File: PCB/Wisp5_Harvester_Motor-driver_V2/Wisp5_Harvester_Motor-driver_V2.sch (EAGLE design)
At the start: 29 parts, among them M1 PINHEAD_PINHD-1X2-1.27MM, M2 PINHEAD_PINHD-1X2-1.27MM, U1 BQ25570

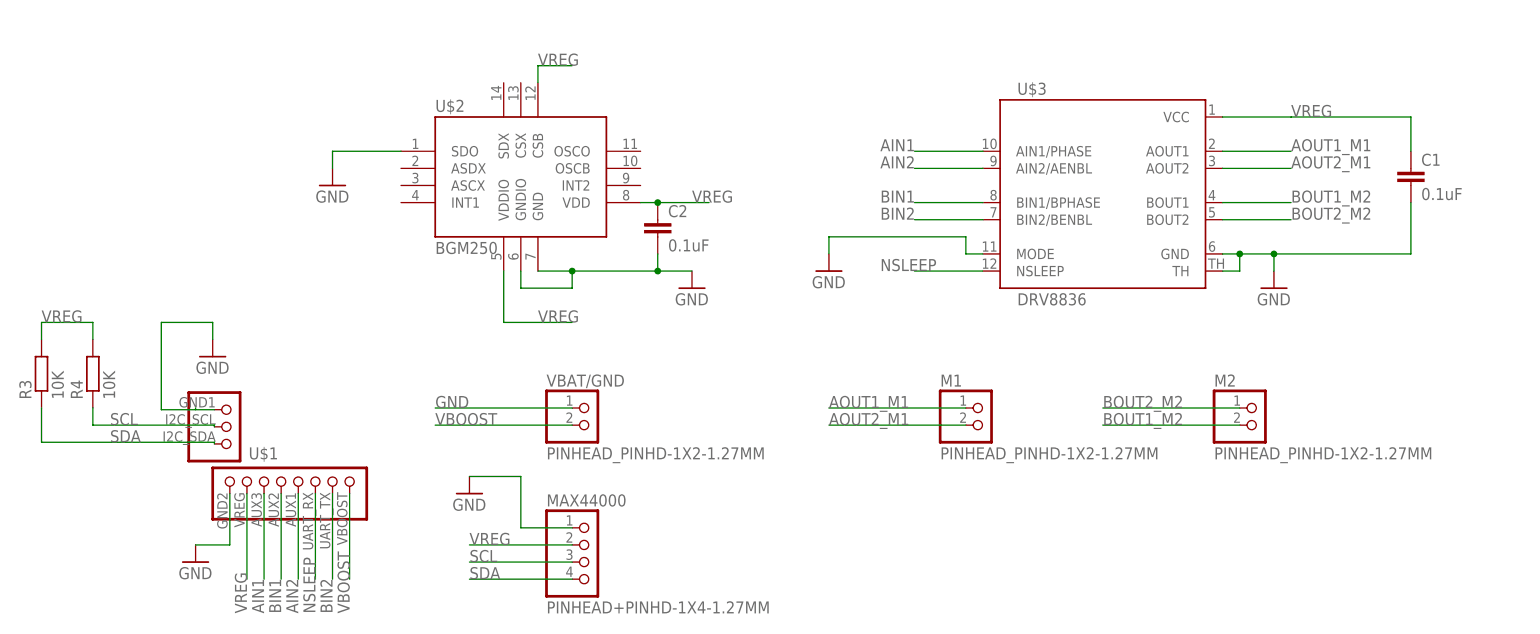
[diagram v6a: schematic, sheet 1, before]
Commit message: Update schematic, added missing scl and sda lines for the gyro
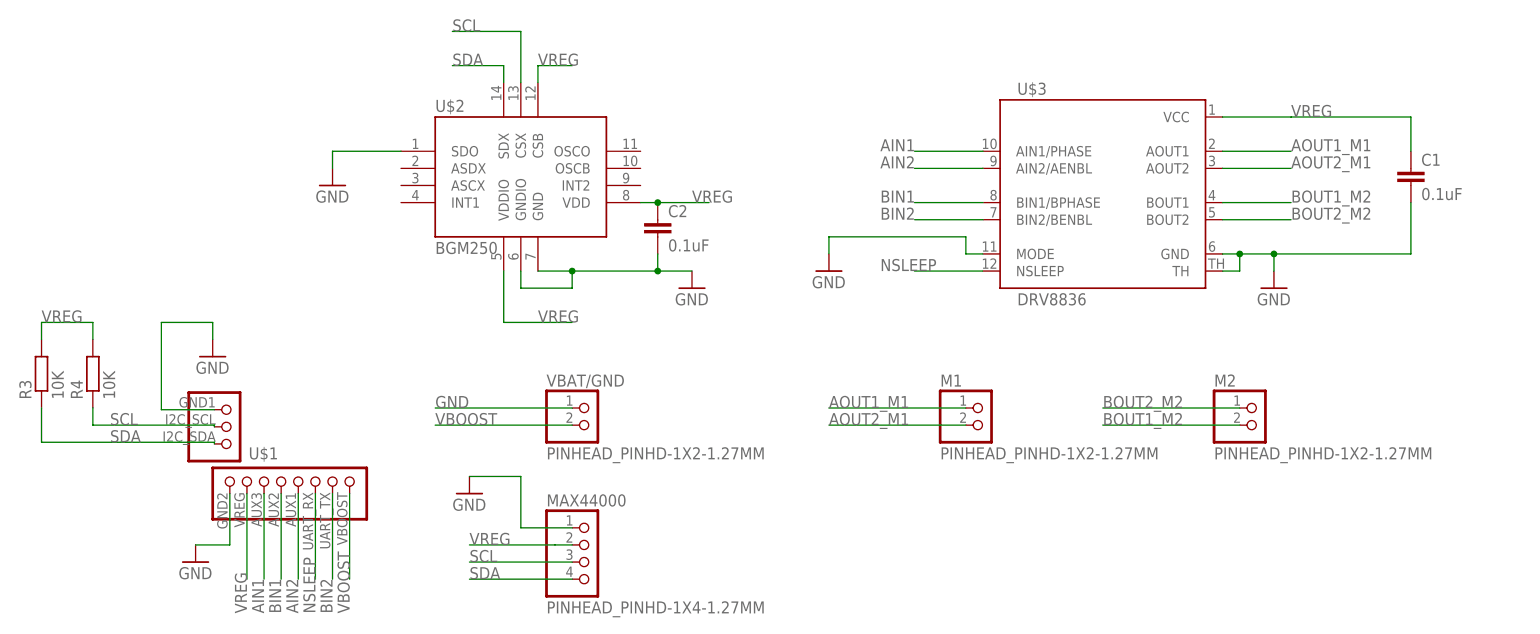
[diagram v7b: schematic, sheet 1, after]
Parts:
- MAX44000: value PINHEAD+PINHD-1X4-1.27MM -> PINHEAD_PINHD-1X4-1.27MM; device Wisp5_Harvester_Motor-driver_V2:PINHEAD+PINHD-1X4-1.27MM -> Wisp5_Harvester_Motor-driver_V2:PINHEAD_PINHD-1X4-1.27MM
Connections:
- net SCL: now also U$2.CSX
- net SDA: now also U$2.SDX
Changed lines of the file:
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@@
 <part name="U$3" library="robot_pcb2" deviceset="DRV8836" device=""/>
 <part name="U1" library="Wisp5_Harvester_Motor-driver_V2" deviceset="BQ25570" device=""/>
-<part name="GND1" library="supply1" deviceset="GND" device=""/>
-<part name="GND5" library="supply1" deviceset="GND" device=""/>
-<part name="C3" library="rcl" deviceset="C-EU" device="C0805" value="4.7uF"/>
-<part name="GND6" library="supply1" deviceset="GND" device=""/>
-<part name="GND7" library="supply1" deviceset="GND" device=""/>
-<part name="C5" library="rcl" deviceset="C-EU" device="C0805" value="10nF"/>
+<part name="GND1" library="supply1" library_urn="urn:adsk.eagle:library:371" deviceset="GND" device=""/>
+<part name="GND5" library="supply1" library_urn="urn:adsk.eagle:library:371" deviceset="GND" device=""/>
+<part name="C3" library="rcl" library_urn="urn:adsk.eagle:library:334" deviceset="C-EU" device="C0805" value="4.7uF"/>
+<part name="GND6" library="supply1" library_urn="urn:adsk.eagle:library:371" deviceset="GND" device=""/>
+<part name="GND7" library="supply1" library_urn="urn:adsk.eagle:library:371" deviceset="GND" device=""/>
+<part name="C5" library="rcl" library_urn="urn:adsk.eagle:library:334" deviceset="C-EU" device="C0805" value="10nF"/>
 <part name="R10" library="resistor" deviceset="R-EU_" device="R0805" value="6.98M"/>
 <part name="R9" library="resistor" deviceset="R-EU_" device="R0805" value="5.76M"/>
-<part name="GND9" library="supply1" deviceset="GND" device=""/>
-<part name="C6" library="rcl" deviceset="C-EU" device="C0805" value="4.7uF"/>
-<part name="C7" library="rcl" deviceset="C-EU" device="C0805" value="0.1 uF"/>
-<part name="GND10" library="supply1" deviceset="GND" device=""/>
-<part name="GND11" library="supply1" deviceset="GND" device=""/>
+<part name="GND9" library="supply1" library_urn="urn:adsk.eagle:library:371" deviceset="GND" device=""/>
+<part name="C6" library="rcl" library_urn="urn:adsk.eagle:library:334" deviceset="C-EU" device="C0805" value="4.7uF"/>
+<part name="C7" library="rcl" library_urn="urn:adsk.eagle:library:334" deviceset="C-EU" device="C0805" value="0.1 uF"/>
+<part name="GND10" library="supply1" library_urn="urn:adsk.eagle:library:371" deviceset="GND" device=""/>
+<part name="GND11" library="supply1" library_urn="urn:adsk.eagle:library:371" deviceset="GND" device=""/>
 <part name="R2" library="resistor" deviceset="R-EU_" device="R0805" value="5.36M"/>
 <part name="R1" library="resistor" deviceset="R-EU_" device="R0805" value="7.50M"/>
@@
 <part name="R7" library="resistor" deviceset="R-EU_" device="R0805" value="3.01M"/>
 <part name="R8" library="resistor" deviceset="R-EU_" device="R0805" value="3.65M"/>
-<part name="GND12" library="supply1" deviceset="GND" device=""/>
-<part name="GND21" library="supply1" deviceset="GND" device=""/>
-<part name="C4" library="rcl" deviceset="C-EU" device="C0805" value="0.1uF"/>
+<part name="GND12" library="supply1" library_urn="urn:adsk.eagle:library:371" deviceset="GND" device=""/>
+<part name="GND21" library="supply1" library_urn="urn:adsk.eagle:library:371" deviceset="GND" device=""/>
+<part name="C4" library="rcl" library_urn="urn:adsk.eagle:library:334" deviceset="C-EU" device="C0805" value="0.1uF"/>
 <part name="C9" library="Wisp5_Harvester_Motor-driver_V2" deviceset="BZ054B223ZSBBQ" device=""/>
 <part name="R3" library="resistor" deviceset="R-EU_" device="R0805" value="10K"/>
 <part name="R4" library="resistor" deviceset="R-EU_" device="R0805" value="10K"/>
-<part name="GND13" library="supply1" deviceset="GND" device=""/>
-<part name="C1" library="rcl" deviceset="C-EU" device="C0805" value="0.1uF"/>
+<part name="GND13" library="supply1" library_urn="urn:adsk.eagle:library:371" deviceset="GND" device=""/>
+<part name="C1" library="rcl" library_urn="urn:adsk.eagle:library:334" deviceset="C-EU" device="C0805" value="0.1uF"/>
 <part name="VIN/GND" library="Wisp5_Harvester_Motor-driver_V2" deviceset="PINHEAD_PINHD-1X2-1.27MM" device=""/>
 <part name="U$1" library="robot_pcb2" deviceset="WISP_HEADER" device=""/>
 <part name="U$2" library="Wisp5_Harvester_Motor-driver_V2" deviceset="BGM250" device=""/>
-<part name="GND2" library="supply1" deviceset="GND" device=""/>
-<part name="GND3" library="supply1" deviceset="GND" device=""/>
-<part name="GND4" library="supply1" deviceset="GND" device=""/>
-<part name="GND8" library="supply1" deviceset="GND" device=""/>
-<part name="GND14" library="supply1" deviceset="GND" device=""/>
+<part name="GND2" library="supply1" library_urn="urn:adsk.eagle:library:371" deviceset="GND" device=""/>
+<part name="GND3" library="supply1" library_urn="urn:adsk.eagle:library:371" deviceset="GND" device=""/>
+<part name="GND4" library="supply1" library_urn="urn:adsk.eagle:library:371" deviceset="GND" device=""/>
+<part name="GND8" library="supply1" library_urn="urn:adsk.eagle:library:371" deviceset="GND" device=""/>
+<part name="GND14" library="supply1" library_urn="urn:adsk.eagle:library:371" deviceset="GND" device=""/>
 <part name="M1" library="Wisp5_Harvester_Motor-driver_V2" deviceset="PINHEAD_PINHD-1X2-1.27MM" device=""/>
 <part name="M2" library="Wisp5_Harvester_Motor-driver_V2" deviceset="PINHEAD_PINHD-1X2-1.27MM" device=""/>
 <part name="VBAT/GND" library="Wisp5_Harvester_Motor-driver_V2" deviceset="PINHEAD_PINHD-1X2-1.27MM" device=""/>
-<part name="C2" library="rcl" deviceset="C-EU" device="C0805" value="0.1uF"/>
-<part name="MAX44000" library="Wisp5_Harvester_Motor-driver_V2" deviceset="PINHEAD+PINHD-1X4-1.27MM" device=""/>
-<part name="GND15" library="supply1" deviceset="GND" device=""/>
+<part name="C2" library="rcl" library_urn="urn:adsk.eagle:library:334" deviceset="C-EU" device="C0805" value="0.1uF"/>
+<part name="GND15" library="supply1" library_urn="urn:adsk.eagle:library:371" deviceset="GND" device=""/>
+<part name="MAX44000" library="Wisp5_Harvester_Motor-driver_V2" deviceset="PINHEAD_PINHD-1X4-1.27MM" device=""/>
 </parts>
 <sheets>
@@
 <instance part="VBAT/GND" gate="G$1" x="83.82" y="33.02"/>
 <instance part="C2" gate="G$1" x="93.98" y="63.5"/>
+<instance part="GND15" gate="1" x="66.04" y="22.86"/>
 <instance part="MAX44000" gate="G$1" x="83.82" y="15.24"/>
-<instance part="GND15" gate="1" x="66.04" y="22.86"/>
 </instances>
 <busses>
@@
 <wire x1="66.04" y1="25.4" x2="73.66" y2="25.4" width="0.1524" layer="91"/>
 <wire x1="73.66" y1="25.4" x2="73.66" y2="17.78" width="0.1524" layer="91"/>
+<wire x1="73.66" y1="17.78" x2="81.28" y2="17.78" width="0.1524" layer="91"/>
 <pinref part="MAX44000" gate="G$1" pin="1"/>
-<wire x1="73.66" y1="17.78" x2="81.28" y2="17.78" width="0.1524" layer="91"/>
 </segment>
 </net>
@@
 </segment>
 <segment>
+<label x="66.04" y="15.24" size="1.778" layer="95"/>
 <pinref part="MAX44000" gate="G$1" pin="2"/>
-<wire x1="81.28" y1="15.24" x2="66.04" y2="15.24" width="0.1524" layer="91"/>
-<label x="66.04" y="15.24" size="1.778" layer="95"/>
+<wire x1="78.74" y1="15.24" x2="66.04" y2="15.24" width="0.1524" layer="91"/>
+<wire x1="81.28" y1="15.24" x2="78.74" y2="15.24" width="0.1524" layer="91"/>
 </segment>
 </net>
@@
 </segment>
 <segment>
-<pinref part="MAX44000" gate="G$1" pin="3"/>
 <wire x1="81.28" y1="12.7" x2="66.04" y2="12.7" width="0.1524" layer="91"/>
 <label x="66.04" y="12.7" size="1.778" layer="95"/>
-</segment>
-</net>
-<net name="N$6" class="0">
-<segment>
-<wire x1="25.4" y1="35.306" x2="25.4" y2="35.56" width="0.1524" layer="91"/>
+<pinref part="MAX44000" gate="G$1" pin="3"/>
+</segment>
+<segment>
+<pinref part="U$2" gate="G$1" pin="CSX"/>
+<wire x1="73.66" y1="83.82" x2="73.66" y2="91.44" width="0.1524" layer="91"/>
+<wire x1="73.66" y1="91.44" x2="63.5" y2="91.44" width="0.1524" layer="91"/>
+<label x="63.5" y="91.44" size="1.778" layer="95"/>
 </segment>
 </net>
@@
 </segment>
 <segment>
-<pinref part="MAX44000" gate="G$1" pin="4"/>
 <wire x1="81.28" y1="10.16" x2="66.04" y2="10.16" width="0.1524" layer="91"/>
 <label x="66.04" y="10.16" size="1.778" layer="95"/>
+<pinref part="MAX44000" gate="G$1" pin="4"/>
+</segment>
+<segment>
+<pinref part="U$2" gate="G$1" pin="SDX"/>
+<wire x1="71.12" y1="83.82" x2="71.12" y2="86.36" width="0.1524" layer="91"/>
+<wire x1="71.12" y1="86.36" x2="63.5" y2="86.36" width="0.1524" layer="91"/>
+<label x="63.5" y="86.36" size="1.778" layer="95"/>
 </segment>
 </net>
@@
 </schematic>
 </drawing>
+<compatibility>
+<note version="8.2" severity="warning">
+Since Version 8.2, Eagle supports online libraries. The ids
+of those online libraries will not be understood (or retained)
+with this version.
+</note>
+</compatibility>
 </eagle>

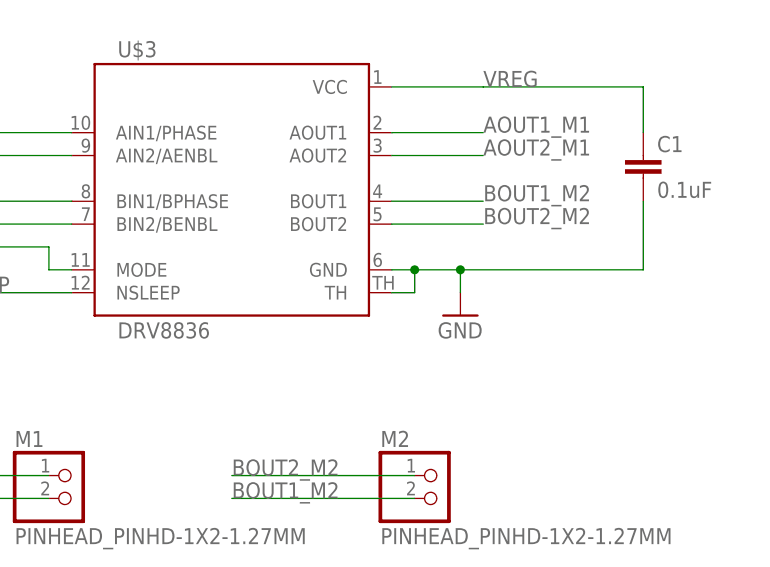
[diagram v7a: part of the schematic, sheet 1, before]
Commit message: Finished routing + fixed drv8836
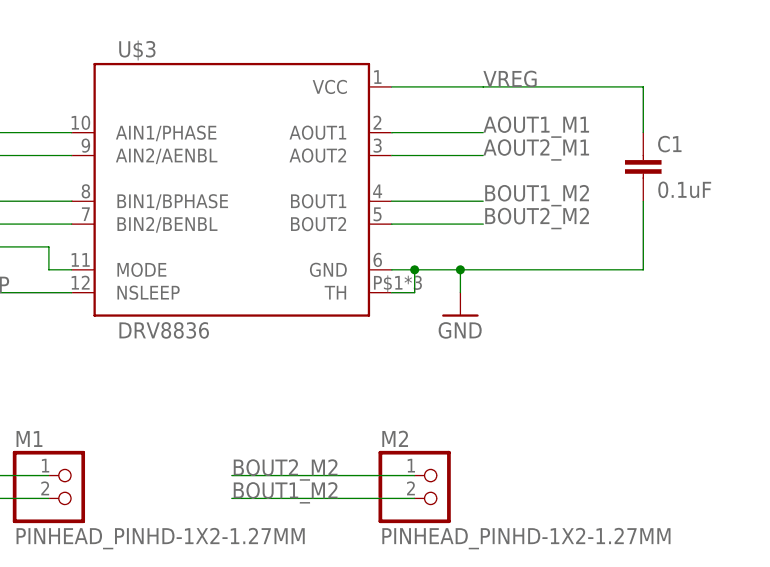
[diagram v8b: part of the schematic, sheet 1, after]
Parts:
- L1, L2: device robot_pcb2:COILCRAFT-LPS4018 -> Wisp5_Harvester_Motor-driver_V2:COILCRAFT-LPS4018
- U$1: device robot_pcb2:WISP_HEADER -> Wisp5_Harvester_Motor-driver_V2:WISP_HEADER
- U$3: device robot_pcb2:DRV8836 -> Wisp5_Harvester_Motor-driver_V2:DRV8836
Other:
- moved on the sheet: U$3
